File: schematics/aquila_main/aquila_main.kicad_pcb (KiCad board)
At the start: 4 copper layers, 98 x 98 mm, 132 parts, among them IC1 MS5611-01BA03, J1 120591-1, J10 PYRO_3, J11 PYRO_2, J12 PYRO_4, J13 AudioJack3_SwitchTR, J14 SERVO, J2 1043P, J3 1043P, J4 PWR, J5 TELEM, J6 GPS, J7 BARO, J8 BMI-S-201, J9 PYRO_1, Q1 IRF7509PbF, Q2 IRF7509PbF, Q3 IRF7509PbF, Q4 IRF7509PbF, U1 LM2576S-3.3/NOPB, U2 LM2576D2TR4-5G, U3 MAX-M8Q, U4 Si4463, U5 B3520, U6 SKY65723-11, U7 ADXL357, U8 BQ29200, U9 Teensy4.1, Y1 30M

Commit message: minor adjustments
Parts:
- moved J2 0.71 mm to (165.5, 100.0)
- moved C10 0.35 mm to (160.0, 59.3)
- moved J3 0.20 mm to (134.5, 100.0)
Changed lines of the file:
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@@
   )
   (footprint "Capacitor_THT:CP_Radial_D8.0mm_P3.50mm" (layer "F.Cu")
-    (at 160 59.652651 90)
+    (at 160 59.3 90)
     (descr "CP, Radial series, Radial, pin pitch=3.50mm, , diameter=8mm, Electrolytic Capacitor")
     (tags "CP Radial series Radial pin pitch 3.50mm  diameter 8mm Electrolytic Capacitor")
@@
   )
   (footprint "aquila:1043" (layer "B.Cu")
-    (at 166 99.5 90)
+    (at 165.5 100 90)
     (property "DigiKey" "36-1043P-ND")
     (property "Sheetfile" "aquila_main.kicad_sch")
@@
   )
   (footprint "aquila:1043" (layer "B.Cu")
-    (at 134.3 100 -90)
+    (at 134.5 100 -90)
     (property "DigiKey" "36-1043P-ND")
     (property "Sheetfile" "aquila_main.kicad_sch")
@@
   (segment (start 179 63) (end 180 62) (width 1) (layer "F.Cu") (net 4))
   (segment (start 180.564971 62) (end 181.100505 62.535534) (width 1) (layer "F.Cu") (net 4))
-  (segment (start 160 59.652651) (end 156.142651 59.652651) (width 0.25) (layer "F.Cu") (net 4))
+  (segment (start 155.79 59.3) (end 160 59.3) (width 0.25) (layer "F.Cu") (net 4))
   (segment (start 157 85) (end 151.5 85) (width 1) (layer "F.Cu") (net 4))
   (segment (start 173.7 68.3) (end 173.7 64.725) (width 0.25) (layer "F.Cu") (net 4))
-  (segment (start 156.142651 59.652651) (end 153 56.51) (width 0.25) (layer "F.Cu") (net 4))
   (segment (start 158 84) (end 157 85) (width 1) (layer "F.Cu") (net 4))
   (segment (start 181.100505 62.899495) (end 181.100505 62.535534) (width 0.25) (layer "F.Cu") (net 4))
@@
   (segment (start 187.464466 64.374703) (end 187.464466 68.899495) (width 1) (layer "F.Cu") (net 4))
   (segment (start 173 69) (end 173.7 68.3) (width 0.25) (layer "F.Cu") (net 4))
+  (segment (start 153 56.51) (end 155.79 59.3) (width 0.25) (layer "F.Cu") (net 4))
   (segment (start 165 84) (end 165 81) (width 1) (layer "F.Cu") (net 4))
   (segment (start 165 84) (end 158 84) (width 1) (layer "F.Cu") (net 4))
@@
   (segment (start 173 69) (end 165 69) (width 1) (layer "B.Cu") (net 4))
   (segment (start 175 69) (end 179 65) (width 1) (layer "B.Cu") (net 4))
-  (segment (start 160 64) (end 160 59.652651) (width 1) (layer "B.Cu") (net 4))
   (segment (start 173 69) (end 175 69) (width 1) (layer "B.Cu") (net 4))
   (segment (start 179 65) (end 179 63) (width 1) (layer "B.Cu") (net 4))
+  (segment (start 160 64) (end 160 59.3) (width 1) (layer "B.Cu") (net 4))
   (segment (start 165 69) (end 160 64) (width 1) (layer "B.Cu") (net 4))
   (segment (start 165 77) (end 173 69) (width 1) (layer "B.Cu") (net 4))

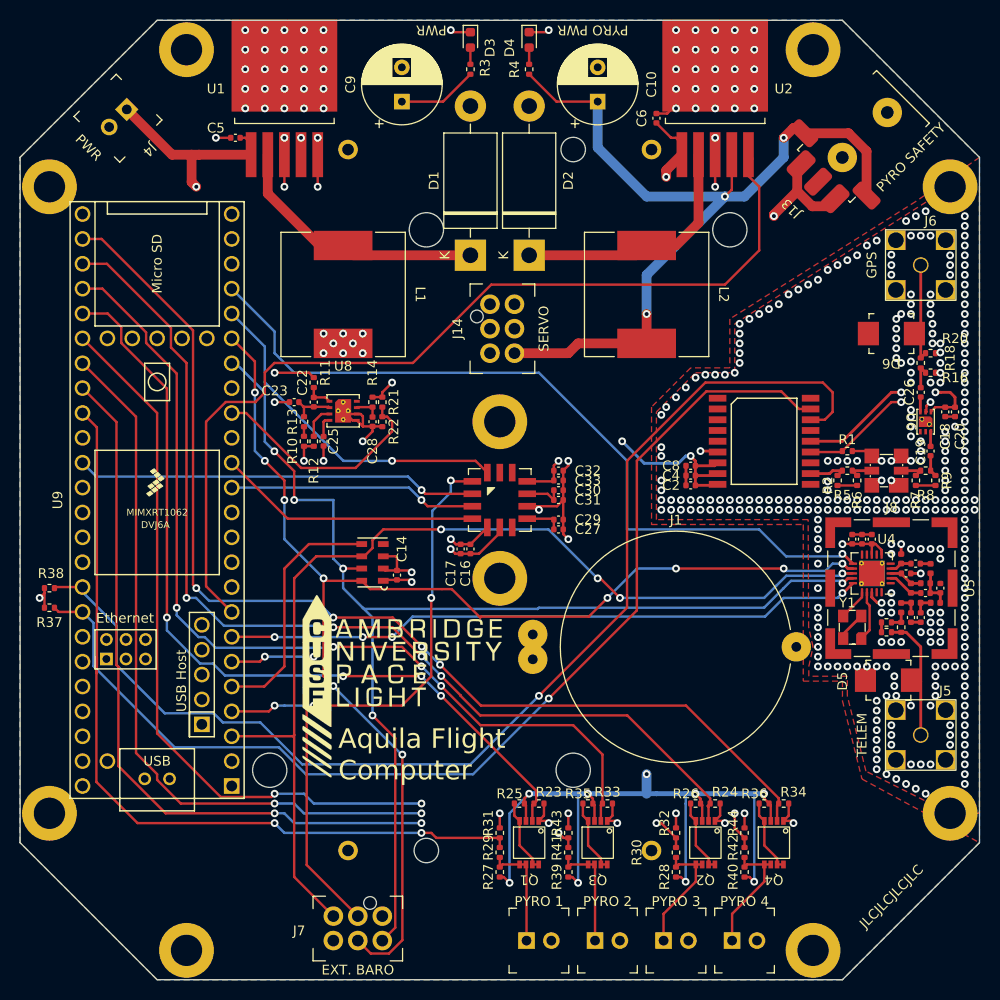
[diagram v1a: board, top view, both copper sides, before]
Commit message: added test points, redesigned power supplies
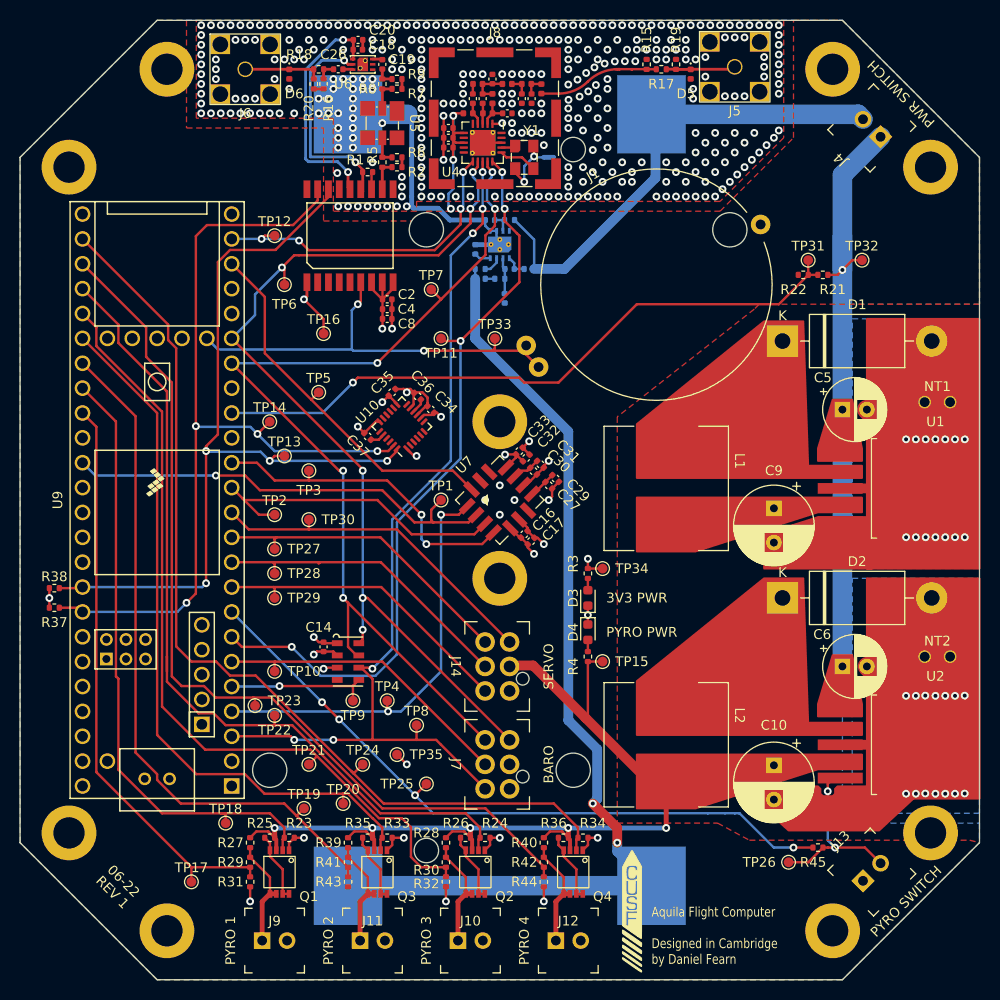
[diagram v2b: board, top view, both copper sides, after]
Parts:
- removed the G*** at (140.0, 119.0)
- added C34: 10n, Capacitor_SMD:C_0402_1005Metric, F.Cu at (142.9, 90.8)
- added C35: 0u1, Capacitor_SMD:C_0402_1005Metric, F.Cu at (139.0, 89.0)
- added C36: 10u, Capacitor_SMD:C_0402_1005Metric, F.Cu at (141.6, 89.4)
- added C37: 2n2, Capacitor_SMD:C_0402_1005Metric, F.Cu at (136.5, 93.5)
- added G***: LOGO, aquila:cusf_logo_small, F.Cu at (163.5, 142.0)
- added NT1: Tie_2, NetTie:NetTie-2_THT_Pad1.0mm, F.Cu at (193.4, 90.0)
- added NT2: Tie_2, NetTie:NetTie-2_THT_Pad1.0mm, F.Cu at (193.4, 116.0)
- added NT3: NetTie_2, NetTie:NetTie-2_SMD_Pad0.5mm, B.Cu at (155.0, 65.0)
- added R45: 4k7, Resistor_SMD:R_0402_1005Metric, F.Cu at (182.5, 135.5)
- added TP1: TestPoint, TestPoint:TestPoint_Pad_D1.0mm, F.Cu at (144.0, 100.0)
- added TP10: TestPoint, TestPoint:TestPoint_Pad_D1.0mm, F.Cu at (127.0, 117.5)
- added TP11: TestPoint, TestPoint:TestPoint_Pad_D1.0mm, F.Cu at (144.0, 83.5)
- added TP12: TestPoint, TestPoint:TestPoint_Pad_D1.0mm, F.Cu at (127.0, 73.0)
- added TP13: TestPoint, TestPoint:TestPoint_Pad_D1.0mm, F.Cu at (128.0, 95.5)
- added TP14: TestPoint, TestPoint:TestPoint_Pad_D1.0mm, F.Cu at (126.5, 92.0)
- added TP15: TestPoint, TestPoint:TestPoint_Pad_D1.0mm, F.Cu at (160.5, 116.5)
- added TP16: TestPoint, TestPoint:TestPoint_Pad_D1.0mm, F.Cu at (132.0, 83.0)
- added TP17: TestPoint, TestPoint:TestPoint_Pad_D1.0mm, F.Cu at (118.5, 139.0)
- added TP18: TestPoint, TestPoint:TestPoint_Pad_D1.0mm, F.Cu at (122.0, 133.0)
- added TP19: TestPoint, TestPoint:TestPoint_Pad_D1.0mm, F.Cu at (130.0, 131.5)
- added TP2: TestPoint, TestPoint:TestPoint_Pad_D1.0mm, F.Cu at (127.0, 101.5)
- added TP20: TestPoint, TestPoint:TestPoint_Pad_D1.0mm, F.Cu at (134.0, 131.0)
- added TP21: TestPoint, TestPoint:TestPoint_Pad_D1.0mm, F.Cu at (130.5, 127.0)
- added TP22: TestPoint, TestPoint:TestPoint_Pad_D1.0mm, F.Cu at (127.0, 122.0)
- added TP23: TestPoint, TestPoint:TestPoint_Pad_D1.0mm, F.Cu at (125.0, 121.0)
- added TP24: TestPoint, TestPoint:TestPoint_Pad_D1.0mm, F.Cu at (136.0, 127.0)
- added TP25: TestPoint, TestPoint:TestPoint_Pad_D1.0mm, F.Cu at (142.5, 129.0)
- added TP26: TestPoint, TestPoint:TestPoint_Pad_D1.0mm, F.Cu at (179.5, 137.0)
- added TP27: TestPoint, TestPoint:TestPoint_Pad_D1.0mm, F.Cu at (127.0, 105.0)
- added TP28: TestPoint, TestPoint:TestPoint_Pad_D1.0mm, F.Cu at (127.0, 107.5)
- added TP29: TestPoint, TestPoint:TestPoint_Pad_D1.0mm, F.Cu at (127.0, 110.0)
- added TP3: TestPoint, TestPoint:TestPoint_Pad_D1.0mm, F.Cu at (130.5, 97.0)
- added TP30: TestPoint, TestPoint:TestPoint_Pad_D1.0mm, F.Cu at (130.5, 102.0)
- added TP31: TestPoint, TestPoint:TestPoint_Pad_D1.0mm, F.Cu at (181.5, 75.5)
- added TP32: TestPoint, TestPoint:TestPoint_Pad_D1.0mm, F.Cu at (187.0, 75.5)
- added TP33: TestPoint, TestPoint:TestPoint_Pad_D1.0mm, F.Cu at (149.5, 83.5)
- added TP34: TestPoint, TestPoint:TestPoint_Pad_D1.0mm, F.Cu at (160.5, 107.0)
- added TP35: TestPoint, TestPoint:TestPoint_Pad_D1.0mm, F.Cu at (139.5, 126.0)
- added TP4: TestPoint, TestPoint:TestPoint_Pad_D1.0mm, F.Cu at (138.5, 120.5)
- added TP5: TestPoint, TestPoint:TestPoint_Pad_D1.0mm, F.Cu at (131.5, 89.0)
- added TP6: TestPoint, TestPoint:TestPoint_Pad_D1.0mm, F.Cu at (128.0, 78.0)
- added TP7: TestPoint, TestPoint:TestPoint_Pad_D1.0mm, F.Cu at (143.0, 78.5)
- added TP8: TestPoint, TestPoint:TestPoint_Pad_D1.0mm, F.Cu at (141.5, 123.0)
- added TP9: TestPoint, TestPoint:TestPoint_Pad_D1.0mm, F.Cu at (135.0, 120.5)
- added U10: MPU-6050, Sensor_Motion:InvenSense_QFN-24_4x4mm_P0.5mm, F.Cu at (140.0, 92.5)
- C22, C23, C25, C28, R10, R11, R12, R13, R14, U8: moved to B.Cu
- C5, C6: footprint Capacitor_SMD:C_0402_1005Metric -> Capacitor_THT:CP_Radial_D6.3mm_P2.50mm
- D5, D6: footprint aquila:DO-214AA -> Diode_SMD:D_0402_1005Metric
- J13: value AudioJack3_SwitchTR -> PYRO_SAFE; footprint aquila:audio_2.5mm_1501_02 -> aquila:MP_2.54_screw_terminal_2x1
- J2, J3: value 1043P -> 1042; footprint aquila:1043 -> aquila:1042
- moved J13 79.1 mm to (188.0, 138.0), turned to 45 degrees
- moved J4 77.0 mm to (188.0, 62.0), turned to 135 degrees
- moved U1 74.1 mm to (190.5, 98.8), turned to -90 degrees
- moved C20 71.9 mm to (135.5, 53.0), turned to 0 degrees
- moved J6 71.8 mm to (124.0, 56.0)
- moved J5 70.8 mm to (174.0, 55.8)
- moved C18 70.5 mm to (135.5, 54.0), turned to 0 degrees
- moved C10 70.1 mm to (178.0, 127.1), turned to -90 degrees
- moved C15 69.3 mm to (149.2, 57.0)
- moved R20 68.7 mm to (131.0, 57.5), turned to -90 degrees
- moved L7 68.7 mm to (150.8, 57.5), turned to 0 degrees
- moved R16 68.7 mm to (132.0, 57.5), turned to -90 degrees
- moved R9 68.6 mm to (139.5, 57.0), turned to 0 degrees
- moved U2 68.5 mm to (190.5, 125.0), turned to -90 degrees
- moved C19 68.5 mm to (138.0, 55.5)
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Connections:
- C10 pad 1: /pyro_sply -> /pyro_pwr
- C10 pad 2: GND -> /batt_n2
- C5 pad 2: GND -> /batt_n1
- C6 pad 2: GND -> /batt_n2
- C9 pad 2: GND -> /batt_n1
- D1 pad 2: GND -> /batt_n1
- D2 pad 2: GND -> /batt_n2
- J14 pad 2: /servo_4 -> /pyro_pwr
- J14 pad 3: /servo_3 -> /servo_4
- J14 pad 4: /servo_2 -> /servo_3
- J14 pad 5: /servo_1 -> /servo_2
- J14 pad 6: /pyro_sply -> /servo_1
- J7 pad 2: /baro_ext_~{cs} -> +3V3
- J7 pad 3: /MISO2 -> /SCLK2
- J7 pad 4: /MOSI2 -> /MISO2
- J7 pad 5: /SCLK2 -> /baro_ext_~{cs}
- J7 pad 6: +3V3 -> /MOSI2
- L2 pad 2: /pyro_sply -> /pyro_pwr
- L4 pad 1: Net-(C13-Pad1) -> Net-(C11-Pad1)
- L4 pad 2: Net-(C11-Pad1) -> Net-(C13-Pad1)
- R11 pad 1: Net-(J2-Pad1) -> Net-(C22-Pad2)
- R11 pad 2: Net-(C22-Pad2) -> Net-(J2-Pad1)
- R14 pad 2: /batt_p -> Net-(J2-Pad1)
- R4 pad 1: /pyro_sply -> /pyro_pwr
- U1 pad 3: GND -> /batt_n1
- U1 pad 5: GND -> /batt_n1
- U2 pad 3: GND -> /batt_n2
- U2 pad 4: /pyro_sply -> /pyro_pwr
- U2 pad 5: /pyro_~{en} -> /pyro_~{on}_off
- U4 pad 2: Net-(C13-Pad1) -> Net-(C11-Pad1)
- U4 pad 3: Net-(C11-Pad1) -> Net-(C13-Pad1)
- U9 pad 11: /servo_3 -> /servo_1
- U9 pad 20: /accel_drdy -> unconnected-(U9-Pad20)
- U9 pad 21: /radio_int -> unconnected-(U9-Pad21)
- U9 pad 22: unconnected-(U9-Pad22) -> /accel_drdy
- U9 pad 23: unconnected-(U9-Pad23) -> /radio_int
- U9 pad 27: /pyro_ch3 -> /pyro_cont4
- U9 pad 28: /pyro_ch2 -> /pyro_ch3
- U9 pad 29: /pyro_ch1 -> /pyro_cont3
- U9 pad 30: /pyro_cont4 -> /pyro_ch2
- U9 pad 31: /pyro_cont3 -> /pyro_cont2
- U9 pad 32: /pyro_cont2 -> /pyro_ch1
- U9 pad 9: /servo_1 -> /servo_3
- Y1 pad 2: GND -> Net-(Y1-Pad2)
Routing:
- net /pyro_sply: track 89.1 -> 0.00 mm, vias 3 -> 0
- net /batt_n1: track 0.00 -> 69.8 mm, vias 0 -> 14
- net /batt_n2: track 0.00 -> 63.1 mm, vias 0 -> 14
- net /radio_int: track 80.9 -> 33.4 mm, vias 1 -> 4
- net /batt_v: track 23.4 -> 67.6 mm, vias 0 -> 1
- net /pyro_pwr: track 153.7 -> 112.5 mm, vias 10 -> 5
- net Net-(J2-Pad1): track 89.7 -> 50.5 mm, vias 1 -> 0
- net /SCLK2: track 132.8 -> 97.2 mm, vias 10 -> 6
- net /SDA: track 119.6 -> 86.1 mm, vias 1 -> 4
- net /bckp_batt: track 78.0 -> 45.8 mm, vias 1 -> 2
- net /batt_p: track 99.3 -> 73.0 mm, vias 3 -> 1
- net /pyro_cont1: track 85.3 -> 59.5 mm, vias 2 -> 0
- net /pyro_~{en}: track 96.3 -> 71.0 mm, vias 0 -> 4
- net Net-(J2-Pad2): track 77.0 -> 102.2 mm, vias 1 -> 2
- net /MOSI2: track 122.6 -> 98.0 mm
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- added copper zone on B.Cu, net /batt_n1
- added copper zone on B.Cu, net /batt_n2
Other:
- board text added: "06-22 REV 1"
- board text added: "3V3 PWR"
- board text added: "Aquila Flight Computer Designed in Cambridge by Daniel Fearn"
- board text added: "BARO"
- board text added: "PWR SWITCH"
- board text added: "PYRO SWITCH"
- board text removed: "Aquila Flight Computer"
- board text removed: "EXT. BARO"
- board text removed: "GPS"
- board text removed: "PWR"
- board text removed: "PYRO SAFETY"
- board text removed: "TELEM"
